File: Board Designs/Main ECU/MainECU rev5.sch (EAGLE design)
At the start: 164 parts, among them Q10 MMBT3904LT3G, Q11 MMBT3904LT3G, Q9 MMBT3904LT3G, X1 CONNECTOR-37, X2 CONNECTOR-4AUTOSPORT, X3 CONNECTOR-4NANO-FIT-VERTICAL-4, X4 CONNECTOR-4NANO-FIT-VERTICAL-4

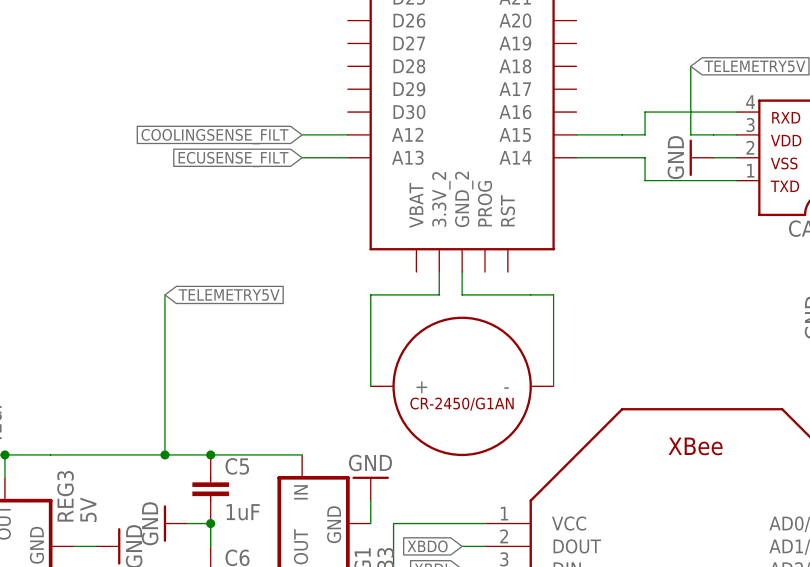
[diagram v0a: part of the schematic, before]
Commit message: Corrected VBAT connection for RTC coin cell
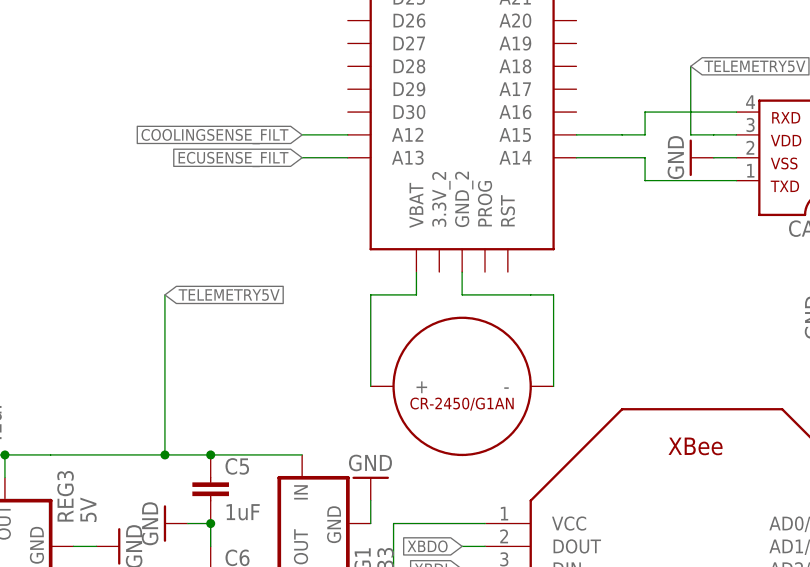
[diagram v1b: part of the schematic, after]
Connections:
- net N$60: now also U$2.VBAT; no longer U$2.3.3V_2
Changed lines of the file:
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@@
 <?xml version="1.0" encoding="utf-8"?>
 <!DOCTYPE eagle SYSTEM "eagle.dtd">
-<eagle version="9.2.2">
+<eagle version="8.6.0">
 <drawing>
 <settings>
@@
 <pinref part="U$16" gate="G$1" pin="+"/>
 <wire x1="441.96" y1="45.72" x2="441.96" y2="55.88" width="0.1524" layer="91"/>
-<wire x1="441.96" y1="55.88" x2="449.58" y2="55.88" width="0.1524" layer="91"/>
-<pinref part="U$2" gate="G$1" pin="3.3V_2"/>
-<wire x1="449.58" y1="55.88" x2="449.58" y2="58.42" width="0.1524" layer="91"/>
+<wire x1="441.96" y1="55.88" x2="447.04" y2="55.88" width="0.1524" layer="91"/>
+<pinref part="U$2" gate="G$1" pin="VBAT"/>
+<wire x1="447.04" y1="55.88" x2="447.04" y2="58.42" width="0.1524" layer="91"/>
 </segment>
 </net>

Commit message: Main ECU rev{1-4}: Add warning about RTC cell assembly, specify current sensor input capacitor value, lower XBee LED resistor to 33R; Main ECU rev{2,4}: Specify MCP3208 input capacitor value; Main ECU rev4: Lower relay-controlling transistors' base resistor to 1k; Main ECU rev5: make all relevant changes previously listed
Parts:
- C10, C9: value (none) -> 0.1uF
- C11: value (none) -> 1uF
- R45: value 2.3k -> 33
- R47, R50: value 2.2k -> 1k
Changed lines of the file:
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@@
 <?xml version="1.0" encoding="utf-8"?>
 <!DOCTYPE eagle SYSTEM "eagle.dtd">
-<eagle version="8.6.0">
+<eagle version="9.2.2">
 <drawing>
 <settings>
@@
 <part name="C7" library="HyTechDevices" deviceset="CAP" device="0805"/>
 <part name="C8" library="HyTechDevices" deviceset="CAP" device="0805"/>
-<part name="C9" library="HyTechDevices" deviceset="CAP" device="0805"/>
-<part name="C10" library="HyTechDevices" deviceset="CAP" device="0805"/>
+<part name="C9" library="HyTechDevices" deviceset="CAP" device="0805" value="0.1uF"/>
+<part name="C10" library="HyTechDevices" deviceset="CAP" device="0805" value="0.1uF"/>
 <part name="GND46" library="HyTechSymbols" deviceset="GND" device=""/>
 <part name="GND47" library="HyTechSymbols" deviceset="GND" device=""/>
@@
 <part name="P+35" library="supply1" library_urn="urn:adsk.eagle:library:371" deviceset="+5V" device=""/>
 <part name="LED14" library="HyTechDevices" deviceset="LED" device="-0805" value="Blue"/>
-<part name="R45" library="HyTechDevices" deviceset="RESISTOR" device="0805-RES" value="2.3k"/>
+<part name="R45" library="HyTechDevices" deviceset="RESISTOR" device="0805-RES" value="33"/>
 <part name="GND62" library="HyTechSymbols" deviceset="GND" device=""/>
 <part name="X3" library="HyTechDevices" deviceset="CONNECTOR-4" device="NANO-FIT-VERTICAL-4"/>
@@
 <part name="GND40" library="HyTechSymbols" deviceset="GND" device=""/>
 <part name="P+32" library="supply1" deviceset="+12V" device=""/>
-<part name="C11" library="HyTechDevices" deviceset="CAP" device="0805"/>
+<part name="C11" library="HyTechDevices" deviceset="CAP" device="0805" value="1uF"/>
 <part name="CAN_TRANSCEIVER2" library="HyTechDevices" deviceset="MCP2551" device="" value="MCP2551"/>
 <part name="GND51" library="HyTechSymbols" deviceset="GND" device=""/>
@@
 <part name="R46" library="HyTechDevices" deviceset="RESISTOR" device="0805-RES" value="120"/>
 <part name="Q9" library="HyTechDevices" deviceset="BJT_NPN" device="SOT" value="MMBT3904LT3G"/>
-<part name="R47" library="HyTechDevices" deviceset="RESISTOR" device="0805-RES" value="2.2k"/>
+<part name="R47" library="HyTechDevices" deviceset="RESISTOR" device="0805-RES" value="1k"/>
 <part name="GND56" library="HyTechSymbols" deviceset="GND" device=""/>
 <part name="Q11" library="HyTechDevices" deviceset="BJT_NPN" device="SOT" value="MMBT3904LT3G"/>
 <part name="GND11" library="HyTechSymbols" deviceset="GND" device=""/>
-<part name="R50" library="HyTechDevices" deviceset="RESISTOR" device="0805-RES" value="2.2k"/>
+<part name="R50" library="HyTechDevices" deviceset="RESISTOR" device="0805-RES" value="1k"/>
 <part name="FLIP" library="supply1" library_urn="urn:adsk.eagle:library:371" deviceset="+5V" device=""/>
 <part name="GND42" library="HyTechSymbols" deviceset="GND" device=""/>
@@
 <wire x1="165.1" y1="165.1" x2="165.1" y2="0" width="0.1524" layer="90"/>
 <text x="165.1" y="165.1" size="3.81" layer="90">Power</text>
-<text x="419.1" y="264.16" size="1.778" layer="97">ECU Current Sensor</text>
-<text x="419.1" y="231.14" size="1.778" layer="97">Cooling Current Sensor</text>
+<text x="416.56" y="264.16" size="1.778" layer="97">ECU Current Sensor</text>
+<text x="416.56" y="231.14" size="1.778" layer="97">Cooling Current Sensor</text>
 <text x="264.16" y="236.22" size="1.778" layer="91">Pullup/down resistors to
 detect open circuit. Install
@@
 <attribute name="VALUE" x="455.676" y="233.299" size="1.778" layer="96" rot="R180"/>
 </instance>
-<instance part="GND46" gate="1" x="452.12" y="233.68" smashed="yes" rot="R270">
-<attribute name="VALUE" x="449.58" y="236.22" size="1.778" layer="96" rot="R270"/>
-</instance>
-<instance part="GND47" gate="1" x="452.12" y="266.7" smashed="yes" rot="R270">
-<attribute name="VALUE" x="449.58" y="269.24" size="1.778" layer="96" rot="R270"/>
+<instance part="GND46" gate="1" x="447.04" y="233.68" smashed="yes" rot="R270">
+<attribute name="VALUE" x="444.5" y="236.22" size="1.778" layer="96" rot="R270"/>
+</instance>
+<instance part="GND47" gate="1" x="447.04" y="266.7" smashed="yes" rot="R270">
+<attribute name="VALUE" x="444.5" y="269.24" size="1.778" layer="96" rot="R270"/>
 </instance>
 <instance part="GND15" gate="1" x="408.94" y="213.36" smashed="yes">
@@
 <pinref part="GND46" gate="1" pin="GND"/>
 <pinref part="C10" gate="G$1" pin="2"/>
-<wire x1="454.66" y1="233.68" x2="457.2" y2="233.68" width="0.1524" layer="91"/>
+<wire x1="449.58" y1="233.68" x2="457.2" y2="233.68" width="0.1524" layer="91"/>
 </segment>
 <segment>
@@
 <pinref part="GND47" gate="1" pin="GND"/>
 <pinref part="C9" gate="G$1" pin="2"/>
-<wire x1="454.66" y1="266.7" x2="457.2" y2="266.7" width="0.1524" layer="91"/>
+<wire x1="449.58" y1="266.7" x2="457.2" y2="266.7" width="0.1524" layer="91"/>
 </segment>
 <segment>
@@
 <pinref part="IMD_SHUTDOWN1" gate="G$1" pin="4"/>
 <wire x1="104.14" y1="210.82" x2="104.14" y2="220.98" width="0.1524" layer="91"/>
-<wire x1="119.38" y1="187.96" x2="147.32" y2="187.96" width="0.1524" layer="91"/>
-<wire x1="147.32" y1="187.96" x2="139.7" y2="187.96" width="0.1524" layer="91"/>
+<wire x1="119.38" y1="187.96" x2="139.7" y2="187.96" width="0.1524" layer="91"/>
+<wire x1="139.7" y1="187.96" x2="147.32" y2="187.96" width="0.1524" layer="91"/>
 <wire x1="139.7" y1="187.96" x2="139.7" y2="200.66" width="0.1524" layer="91"/>
 <junction x="104.14" y="210.82"/>
 <pinref part="R17" gate="G$1" pin="1"/>
-<junction x="147.32" y="187.96"/>
 <label x="111.76" y="210.82" size="1.778" layer="95"/>
 <wire x1="139.7" y1="200.66" x2="139.7" y2="210.82" width="0.1524" layer="91"/>
@@
 <wire x1="132.08" y1="200.66" x2="139.7" y2="200.66" width="0.1524" layer="91"/>
 <junction x="139.7" y="200.66"/>
+<junction x="139.7" y="187.96"/>
 </segment>
 </net>
